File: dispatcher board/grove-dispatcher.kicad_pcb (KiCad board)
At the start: 2 copper layers, 156.8 x 75.6 mm, 75 parts, among them P1 CONN_01X12, P10 CONN_01X06, P11 CONN_01X06, P12 CONN_01X06, P13 CONN_01X06, P14 CONN_01X06, P15 CONN_01X06, P16 CONN_01X06, P17 CONN_01X06, P2 CONN_01X06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

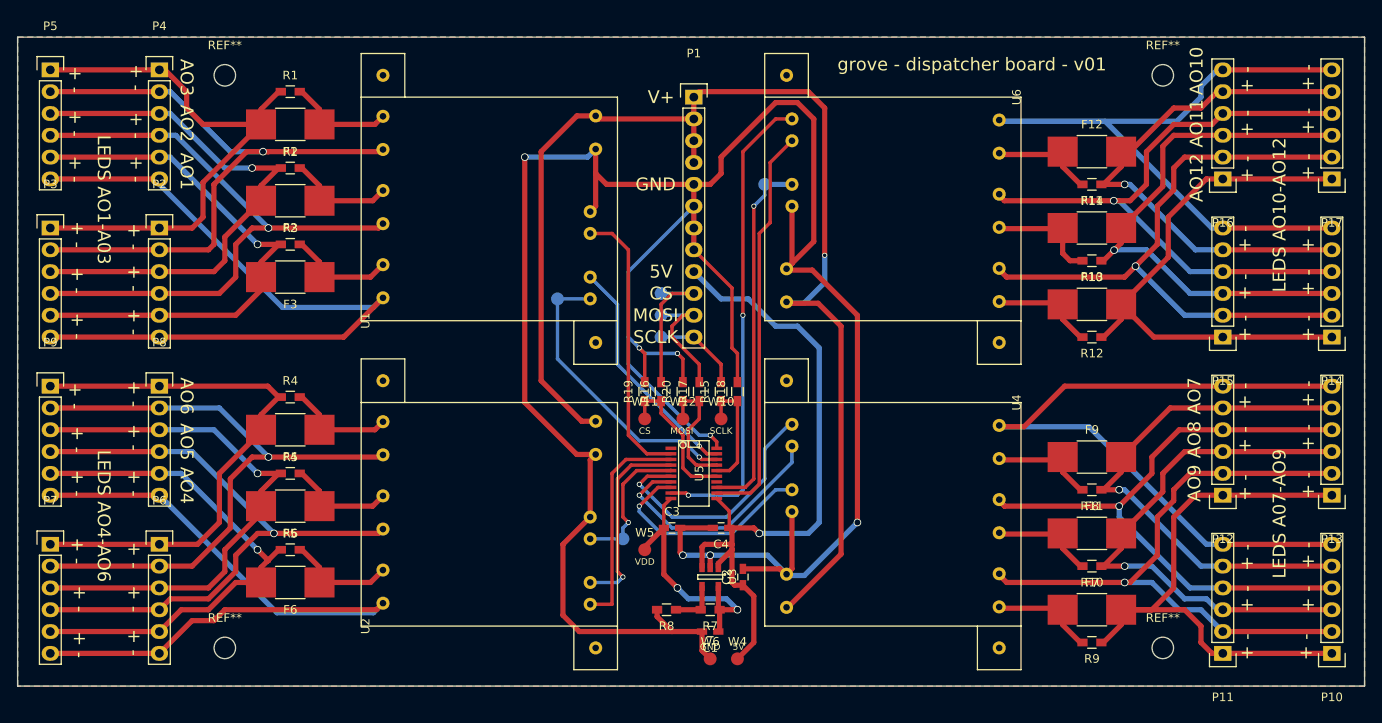
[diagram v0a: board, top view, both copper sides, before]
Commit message: Small correction to the pico buck mounting holes
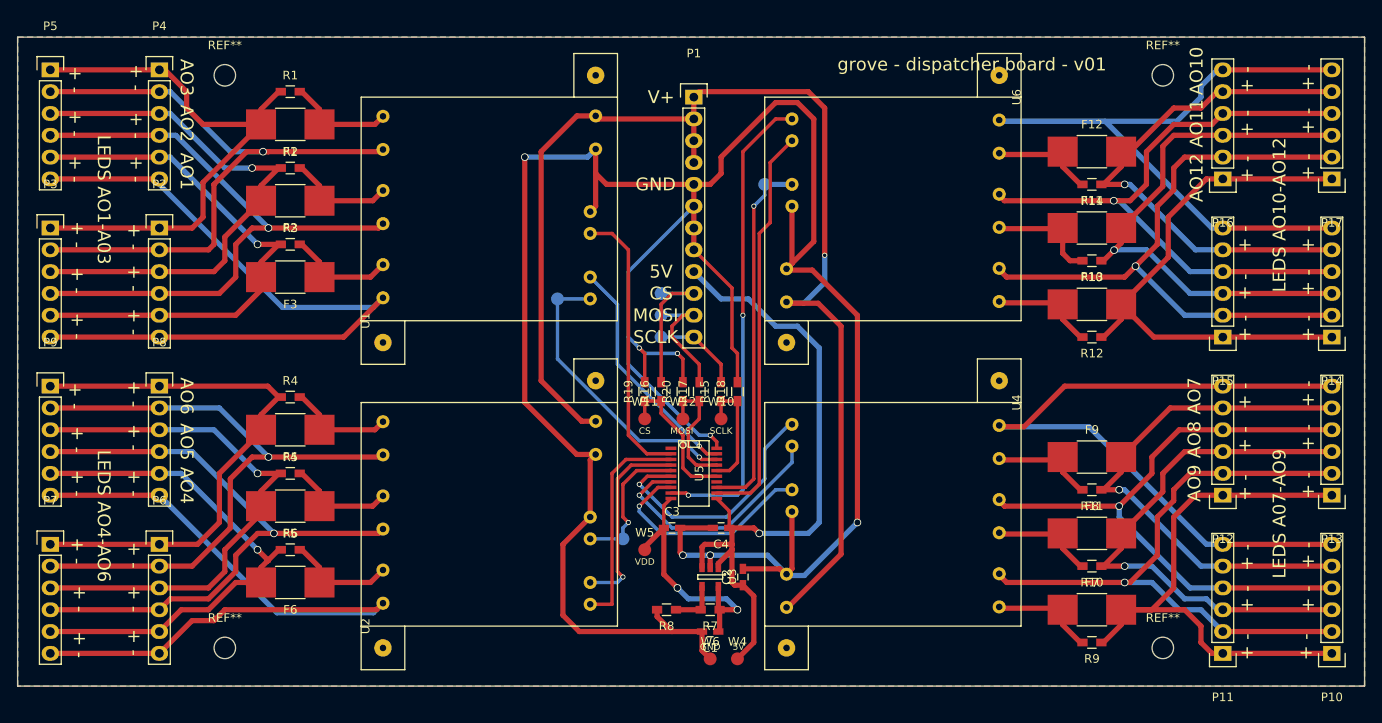
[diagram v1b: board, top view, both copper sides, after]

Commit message: Rename some nets for debug/documentation
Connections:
- net Net-(R15-Pad1) renamed /SCLK_IN
- net Net-(R16-Pad1) renamed /CS_IN
- net Net-(R17-Pad1) renamed /MOSI_IN
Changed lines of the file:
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@@
     (links 204)
     (no_connects 0)
-    (area 60.296667 54.735 219.738334 134.98)
+    (area 61.544999 57.099999 218.490001 132.765001)
     (thickness 1.6)
     (drawings 81)
@@
   (net 55 /AO11)
   (net 56 /AO12)
-  (net 57 "Net-(R15-Pad1)")
-  (net 58 "Net-(R16-Pad1)")
-  (net 59 "Net-(R17-Pad1)")
+  (net 57 /SCLK_IN)
+  (net 58 /CS_IN)
+  (net 59 /MOSI_IN)
   (net_class Default "This is the default net class."
     (clearance 0.2)
@@
     (add_net /AO9)
     (add_net /CS_5V)
+    (add_net /CS_IN)
     (add_net /MOSI_5V)
+    (add_net /MOSI_IN)
     (add_net /SCLK_5V)
+    (add_net /SCLK_IN)
     (add_net /V+)
     (add_net GND)
@@
     (add_net "Net-(P6-Pad4)")
     (add_net "Net-(P6-Pad6)")
-    (add_net "Net-(R15-Pad1)")
-    (add_net "Net-(R16-Pad1)")
-    (add_net "Net-(R17-Pad1)")
     (add_net "Net-(R7-Pad2)")
   )
@@
     (pad 14 smd rect (at 0.9906 -2.667 270) (size 0.4064 1.27) (layers F.Cu F.Paste F.Mask))
     (pad 15 smd rect (at 0.3302 -2.667 270) (size 0.4064 1.27) (layers F.Cu F.Paste F.Mask)
-      (net 58 "Net-(R16-Pad1)"))
+      (net 58 /CS_IN))
     (pad 16 smd rect (at -0.3302 -2.667 270) (size 0.4064 1.27) (layers F.Cu F.Paste F.Mask)
-      (net 57 "Net-(R15-Pad1)"))
+      (net 57 /SCLK_IN))
     (pad 17 smd rect (at -0.9652 -2.667 270) (size 0.4064 1.27) (layers F.Cu F.Paste F.Mask)
-      (net 59 "Net-(R17-Pad1)"))
+      (net 59 /MOSI_IN))
     (pad 18 smd rect (at -1.6256 -2.667 270) (size 0.4064 1.27) (layers F.Cu F.Paste F.Mask)
       (net 47 /AO1))
@@
     (fp_line (start -0.5 -0.675) (end 0.5 -0.675) (layer F.SilkS) (width 0.15))
     (pad 1 smd rect (at -1.1 0 90) (size 1.2 0.9) (layers F.Cu F.Paste F.Mask)
-      (net 57 "Net-(R15-Pad1)"))
+      (net 57 /SCLK_IN))
     (pad 2 smd rect (at 1.1 0 90) (size 1.2 0.9) (layers F.Cu F.Paste F.Mask)
       (net 36 /SCLK_5V))
@@
     (fp_line (start -0.5 -0.675) (end 0.5 -0.675) (layer F.SilkS) (width 0.15))
     (pad 1 smd rect (at -1.1 0 90) (size 1.2 0.9) (layers F.Cu F.Paste F.Mask)
-      (net 58 "Net-(R16-Pad1)"))
+      (net 58 /CS_IN))
     (pad 2 smd rect (at 1.1 0 90) (size 1.2 0.9) (layers F.Cu F.Paste F.Mask)
       (net 38 /CS_5V))
@@
     (fp_line (start -0.5 -0.675) (end 0.5 -0.675) (layer F.SilkS) (width 0.15))
     (pad 1 smd rect (at -1.1 0 90) (size 1.2 0.9) (layers F.Cu F.Paste F.Mask)
-      (net 59 "Net-(R17-Pad1)"))
+      (net 59 /MOSI_IN))
     (pad 2 smd rect (at 1.1 0 90) (size 1.2 0.9) (layers F.Cu F.Paste F.Mask)
       (net 37 /MOSI_5V))
@@
     (fp_line (start -0.5 -0.675) (end 0.5 -0.675) (layer F.SilkS) (width 0.15))
     (pad 1 smd rect (at -1.1 0 90) (size 1.2 0.9) (layers F.Cu F.Paste F.Mask)
-      (net 57 "Net-(R15-Pad1)"))
+      (net 57 /SCLK_IN))
     (pad 2 smd rect (at 1.1 0 90) (size 1.2 0.9) (layers F.Cu F.Paste F.Mask)
       (net 26 GND))
@@
     (fp_line (start -0.5 -0.675) (end 0.5 -0.675) (layer F.SilkS) (width 0.15))
     (pad 1 smd rect (at -1.1 0 90) (size 1.2 0.9) (layers F.Cu F.Paste F.Mask)
-      (net 58 "Net-(R16-Pad1)"))
+      (net 58 /CS_IN))
     (pad 2 smd rect (at 1.1 0 90) (size 1.2 0.9) (layers F.Cu F.Paste F.Mask)
       (net 26 GND))
@@
     (fp_line (start -0.5 -0.675) (end 0.5 -0.675) (layer F.SilkS) (width 0.15))
     (pad 1 smd rect (at -1.1 0 90) (size 1.2 0.9) (layers F.Cu F.Paste F.Mask)
-      (net 59 "Net-(R17-Pad1)"))
+      (net 59 /MOSI_IN))
     (pad 2 smd rect (at 1.1 0 90) (size 1.2 0.9) (layers F.Cu F.Paste F.Mask)
       (net 26 GND))
@@
     (fp_circle (center 0 0) (end 1 0) (layer F.CrtYd) (width 0.05))
     (pad 1 smd circle (at 0 0) (size 1.5 1.5) (layers F.Cu F.Mask)
-      (net 57 "Net-(R15-Pad1)"))
+      (net 57 /SCLK_IN))
   )
   (module Measurement_Points:Measurement_Point_Round-SMD-Pad_Small (layer F.Cu)
@@
     (fp_circle (center 0 0) (end 1 0) (layer F.CrtYd) (width 0.05))
     (pad 1 smd circle (at 0 0) (size 1.5 1.5) (layers F.Cu F.Mask)
-      (net 58 "Net-(R16-Pad1)"))
+      (net 58 /CS_IN))
   )
   (module Measurement_Points:Measurement_Point_Round-SMD-Pad_Small (layer F.Cu)
@@
     (fp_circle (center 0 0) (end 1 0) (layer F.CrtYd) (width 0.05))
     (pad 1 smd circle (at 0 0) (size 1.5 1.5) (layers F.Cu F.Mask)
-      (net 59 "Net-(R17-Pad1)"))
+      (net 59 /MOSI_IN))
   )
   (module Mounting_Holes:MountingHole_2.5mm (layer F.Cu)

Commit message: Update skilscreens
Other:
- board text added: "CS_IN"
- board text added: "MOSI_IN"
- board text added: "SCLK_IN"
